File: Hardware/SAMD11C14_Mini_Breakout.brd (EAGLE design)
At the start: 160 x 100 mm, 34 parts, among them J1 USB, J2 USB_A_PTH_MALE, J5 QWIIC, Q1 2.5A/30V/105mΩ, Q2 310mA/60V/1.6Ω, U1 ATSAMD11C14, U2 3.3V, Y1 DNP

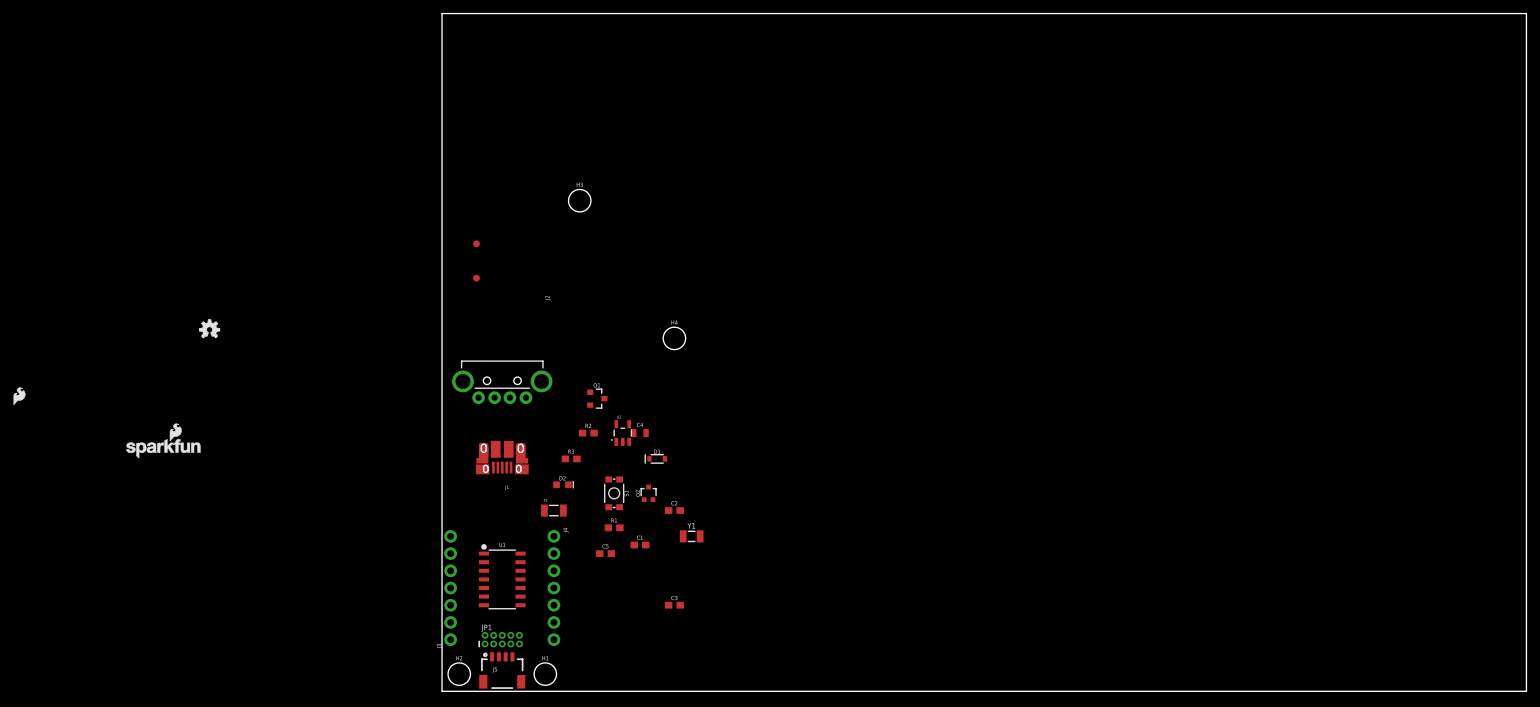
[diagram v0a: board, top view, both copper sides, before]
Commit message: Changed up schematic to have less parts. Moved parts on board around
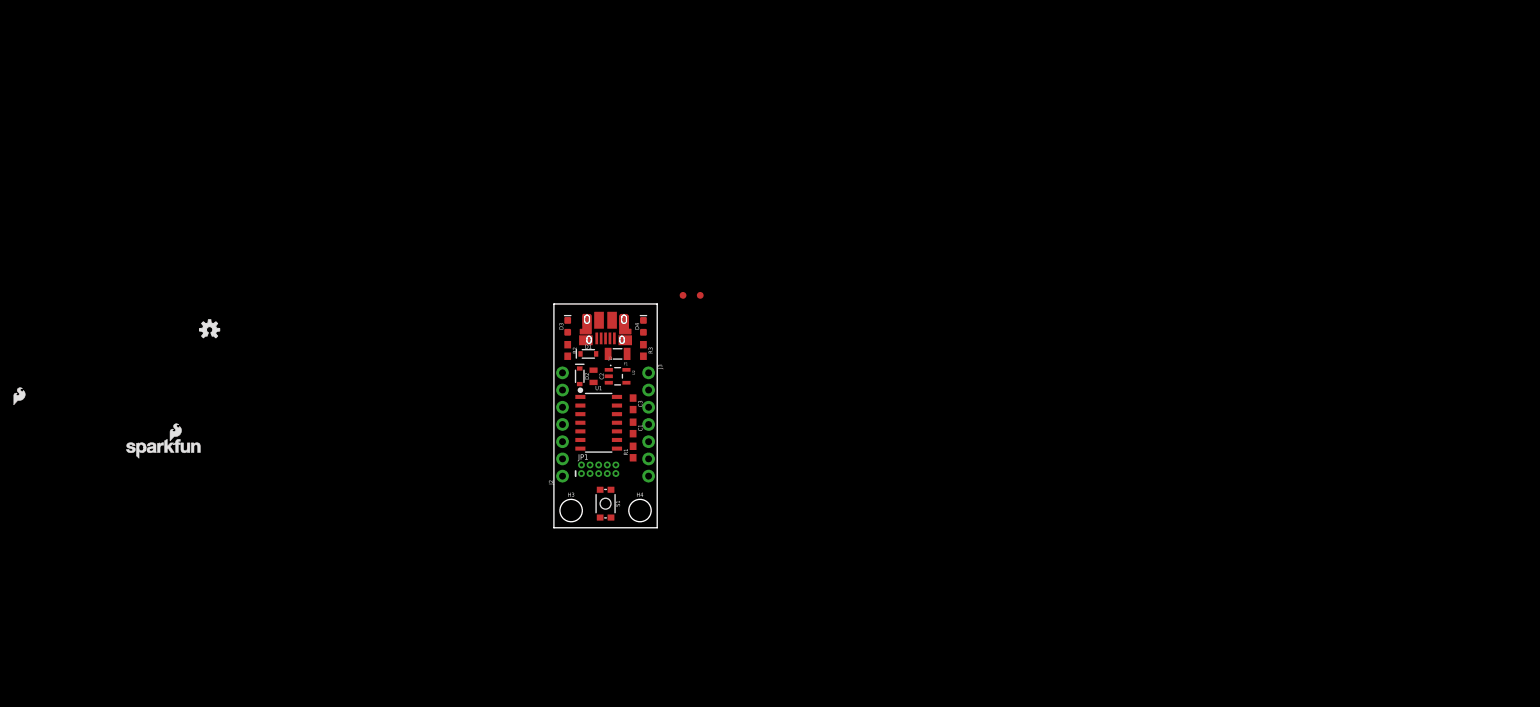
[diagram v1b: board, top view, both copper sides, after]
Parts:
- removed C4: 1.0uF, SparkFun-Capacitors:0805
- removed C5: 2.2uF, SparkFun-Capacitors:0603
- removed H1, H2: STAND-OFF, SparkFun-Hardware:STAND-OFF
- removed J4: (no value), SparkFun-Connectors:1X07_NO_SILK
- removed J5: QWIIC, SparkFun-Connectors:1X04_1MM_RA
- removed Q1: 2.5A/30V/105mΩ, SparkFun-DiscreteSemi:SOT23-3
- removed Q2: 310mA/60V/1.6Ω, SparkFun-DiscreteSemi:SOT323
- removed Y1: DNP, samd21-temp:CRYSTAL-SMD-3.2X1.5MM
- added D3: BLUE, SparkFun-LED:LED-0603
- added D4: RED, SparkFun-LED:LED-0603
- C2: value DNP -> 1.0uF; device SparkFun-Capacitors:0603 -> SparkFun-Capacitors:0805
- C3: value DNP -> 2.2uF
- D2: value BLUE -> 1A/23V/620mV; device SparkFun-LED:LED-0603 -> SparkFun-DiscreteSemi:SOD-323
- J2: value USB_A_PTH_MALE -> (none); device SparkFun-Connectors:USB-A-H -> SparkFun-Connectors:1X07_NO_SILK
- R2: value 100k -> 330
- moved J3 49.0 mm to (30.5, 47.0), turned to 270 degrees
- moved H3 45.7 mm to (19.1, 26.7)
- moved FD1 33.9 mm to (38.1, 58.4)
- moved FD2 30.6 mm to (35.6, 58.4)
- moved C3 30.3 mm to (28.2, 42.4), turned to 270 degrees
- moved JP1 28.9 mm to (23.1, 32.8)
- moved U1 27.1 mm to (23.1, 39.6)
- moved H4 25.9 mm to (29.2, 26.7)
- moved F1 25.0 mm to (25.9, 49.8), turned to 180 degrees
- moved J1 24.4 mm to (24.1, 52.1)
- moved C2 23.1 mm to (22.4, 46.5), turned to 270 degrees
- moved R3 19.2 mm to (29.7, 50.3), turned to 270 degrees
- moved D1 18.5 mm to (21.6, 49.8)
- moved C1 17.3 mm to (28.2, 38.9), turned to 270 degrees
- moved J2 16.6 mm to (17.8, 31.8), turned to 90 degrees
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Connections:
- removed net A15\: U1.5
- removed net N$3: D2.C, Q2.3
- net !RESET: now also J2.1; no longer J3.7
- net 3.3V: now also C3.1, J3.2; no longer C5.1, J4.2, J5.2
- net A14: now also J3.6; no longer J4.4, J5.3
- net A15: now also J3.7, U1.5; no longer J4.3, J5.4
- net A2: now also J3.3; no longer J4.7
- net A4: now also J3.4; no longer J4.6
- net A5: now also J3.5, R2.2; no longer J4.5, Q2.1
- net D30: now also J2.3; no longer J3.2
- net D31: now also J2.2; no longer J3.1
- net D8: now also J2.5; no longer C2.2, J3.4, Y1.P$2
- net D9: now also J2.4; no longer C3.2, J3.3, Y1.P$1
- net GND: now also C2.2, C3.2, D3.C, D4.C, J2.6; no longer C2.1, C3.1, C4.2, C5.2, J2.GND, J3.5, J5.1, Q2.2, R2.1
- net N$1: now also D3.A, R2.1; no longer D2.A, R3.1
- net N$2: now also D4.A, R3.1; no longer Q1.1, R2.2
- net N$4: no longer J2.VBUS
- net USB_D+: no longer J2.D+
- net USB_D-: no longer J2.D-
- net VIN: now also C2.1, D2.C; no longer C4.1, J4.1, Q1.2
- net V_BATT: now also D2.A, J2.7; no longer J3.6, Q1.3
- net V_USB: now also J3.1
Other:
- board size 160 x 100 mm -> 15.2 x 33 mm

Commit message: Finished layout for v01
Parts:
- added JP2, JP3: JUMPER-SMT_2_NC_TRACE_NO-SILK, SparkFun-Jumpers:SMT-JUMPER_2_NC_TRACE_NO-SILK
- added U$1: (no value), buzzard_labels:#RST4
- added U$10: (no value), buzzard_labels:A1412
- added U$11: (no value), buzzard_labels:A1513
- added U$12: (no value), buzzard_labels:GND1
- added U$13: (no value), buzzard_labels:VBAT0
- added U$14: (no value), buzzard_labels:VUSB2
- added U$2: (no value), buzzard_labels:3V33
- added U$3: (no value), buzzard_labels:85
- added U$4: (no value), buzzard_labels:96
- added U$5: (no value), buzzard_labels:307
- added U$6: (no value), buzzard_labels:318
- added U$7: (no value), buzzard_labels:A29
- added U$8: (no value), buzzard_labels:A410
- added U$9: (no value), buzzard_labels:A511
- moved LOGO3 82.6 mm to (9.40, 3.05)
- moved FRAME2 72.4 mm to (-17.5, -11.2)
- moved FRAME1 68.3 mm to (-17.5, -11.2)
- moved LOGO2 62.1 mm to (14.2, 23.9), flipped to the bottom
- moved FD1 57.6 mm to (14.5, 5.84)
- moved LOGO1 47.6 mm to (7.62, 30.7), flipped to the bottom
- moved FD2 43.5 mm to (1.02, 32.0)
- moved D1 29.9 mm to (5.08, 24.9)
- moved F1 29.5 mm to (10.2, 24.9)
- moved D2 29.4 mm to (3.81, 22.1)
- moved U2 29.2 mm to (10.2, 21.8)
- moved H3 29.2 mm to (2.54, 2.54)
- moved H4 29.2 mm to (12.7, 2.54)
- moved R2 29.2 mm to (2.03, 26.2), turned to 90 degrees
- moved U1 29.2 mm to (6.60, 15.5)
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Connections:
- new net N$3: D4.A, JP3.1
- new net N$5: D4.C, R3.2
- net 3.3V: now also JP3.2; no longer R3.2
- net A5: now also JP2.2; no longer R2.2
- net GND: now also R2.1, R3.1; no longer D3.C, D4.C
- net N$1: now also JP2.1; no longer R2.1
- net N$2: now also D3.C, R2.2; no longer D4.A, R3.1
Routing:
- net A5: track 0.00 -> 43.1 mm, vias 0 -> 3
- net 3.3V: track 0.00 -> 37.8 mm, vias 0 -> 2
- net !RESET: track 0.00 -> 29.1 mm
- net USB_D+: track 0.00 -> 17.6 mm, vias 0 -> 2
- net USB_D-: track 0.00 -> 17.5 mm, vias 0 -> 2
- net A14: track 0.00 -> 13.3 mm, vias 0 -> 1
- net A15: track 0.00 -> 13.2 mm, vias 0 -> 1
- net A4: track 0.00 -> 11.5 mm, vias 0 -> 1
- net V_USB: track 0.00 -> 9.99 mm, vias 0 -> 1
- net VIN: track 0.00 -> 9.79 mm
- net D31: track 0.00 -> 9.40 mm, vias 0 -> 1
- net A2: track 0.00 -> 7.63 mm, vias 0 -> 1
- net D30: track 0.00 -> 6.75 mm
- net N$4: track 0.00 -> 5.18 mm
- net N$3: track 0.00 -> 4.14 mm, vias 0 -> 1
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- added copper zone on layer 1, net GND
- added copper zone on layer 16, net GND
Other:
- board text added: "!RST"
- board text added: "30"
- board text added: "31"
- board text added: "3V3"
- board text added: "8"
- board text added: "9"
- board text added: "A14"
- board text added: "A15"
- board text added: "A2"
- board text added: "A4"
- board text added: "A5"
- board text added: "GND"
- board text added: "JP2"
- board text added: "JP3"
- board text added: "LED"
- board text added: "PWR"
- board text added: "SAMD11C Mini Breakout"
- board text added: "Shawn Hymel"
- board text added: "VBAT"
- board text added: "VUSB"
- board text added: "v10"
